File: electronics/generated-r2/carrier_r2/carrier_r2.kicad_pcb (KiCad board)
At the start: 2 copper layers, 100 x 140 mm, 40 parts, among them J1 EXTERNAL_3V3_FUSED_1A, J2 ENCODER_BANK_0, J3 ENCODER_BANK_1, J4 ENCODER_BANK_2, J5 ENCODER_BANK_3, J6 ADXL355_MODULE, J7 ODOMETER_3V3_ONLY, J8 ADC_BANK_FANOUT, J9 INTERLOCK_GND_LIFT_PG_REMOTE_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, Q1 MMBT3904, U1 Raspberry_Pi_Pico_USB_powered, U2 SN74LVC244APWR, U3 SN74LVC244APWR, U4 SN74LVC125AD_IOFF

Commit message: build(r2): publish final routed electronics and checks [skip ci]
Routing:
- net GND: track 552.7 -> 481.0 mm
- net P_MOSI1: track 108.6 -> 129.9 mm
- net LIFT_STOWED_N: track 108.3 -> 90.8 mm, vias 0 -> 1
- net SENS_3V3: track 294.4 -> 281.1 mm, vias 1 -> 2
- net MISO0: track 96.3 -> 85.4 mm, vias 1 -> 2
- net ADC_CS3: track 65.6 -> 75.8 mm
- net ADC_CS2: track 65.1 -> 73.8 mm, vias 1 -> 3
- net MISO0_RAW: track 110.2 -> 118.5 mm, vias 3 -> 1
- net P_SCK1: track 112.6 -> 105.2 mm
- net ADC_CS1: track 64.7 -> 70.6 mm, vias 1 -> 3
- net POWER_GOOD: track 105.1 -> 110.9 mm, vias 0 -> 1
- net ADC_CS0: track 68.5 -> 74.1 mm
- net P_CS2: track 43.4 -> 48.9 mm
- net PICO_3V3: track 192.2 -> 188.6 mm
- net CS3: track 52.8 -> 55.8 mm
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
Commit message: build(r2): publish four routed boards and checks [skip ci]
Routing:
- net MISO0_RAW: track 118.5 -> 150.0 mm, vias 1 -> 0
- net P_MOSI1: track 129.9 -> 106.6 mm, vias 1 -> 2
- net ADC_CS1: track 70.6 -> 84.1 mm, vias 3 -> 1
- net PICO_3V3: track 188.6 -> 176.4 mm
- net MISO0: track 85.4 -> 96.3 mm, vias 2 -> 1
- net P_SCK1: track 105.2 -> 114.6 mm
- net LIFT_STOWED_N: track 90.8 -> 99.2 mm
- net CS2: track 46.5 -> 54.7 mm
- net SENS_3V3: track 281.1 -> 273.2 mm, vias 2 -> 1
- net P_CS2: track 48.9 -> 42.1 mm
- net CS_ADXL: track 79.4 -> 84.3 mm
- net ADC_CS3: track 75.8 -> 71.9 mm
- net CS1: track 47.2 -> 50.1 mm
- net CS3: track 55.8 -> 53.1 mm
- net ADC_CS0: track 74.1 -> 71.6 mm, vias 1 -> 0
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
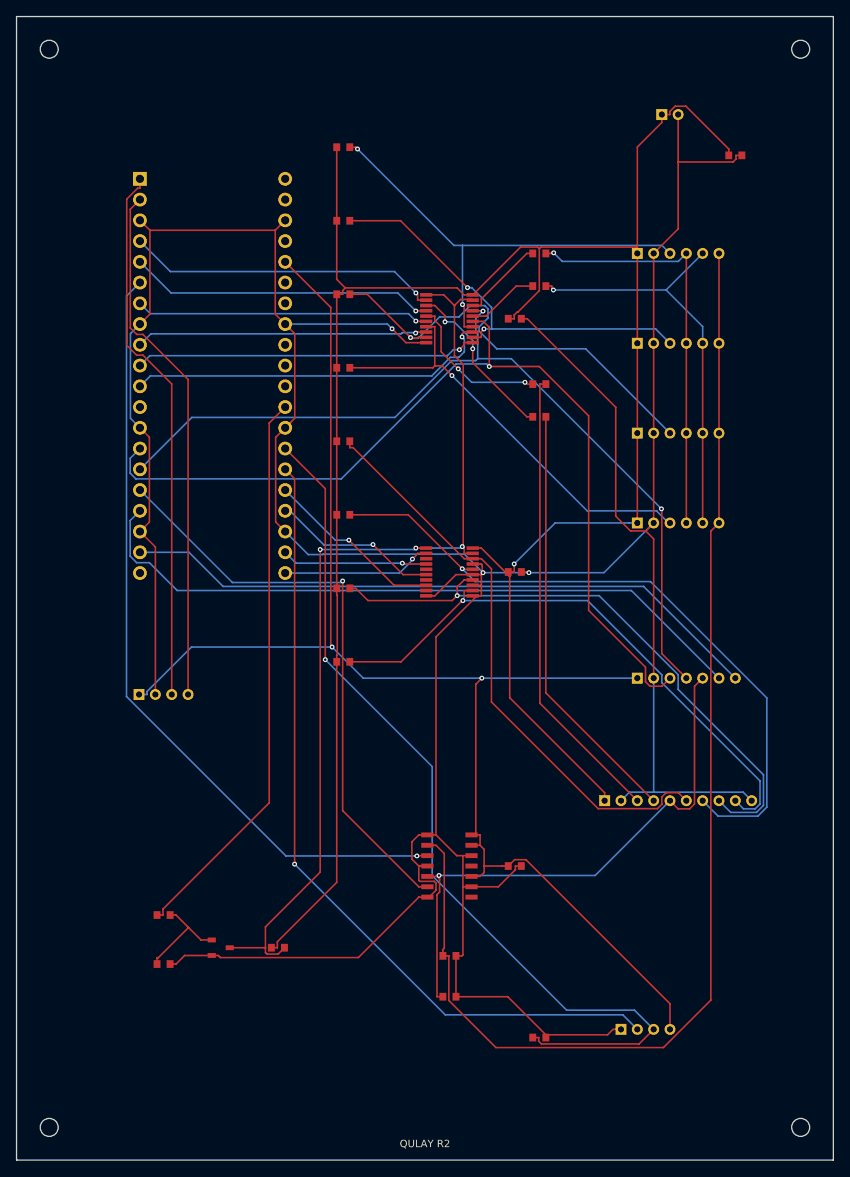
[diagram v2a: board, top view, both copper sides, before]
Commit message: build(r2): publish verified four-board electronics baseline [skip ci]
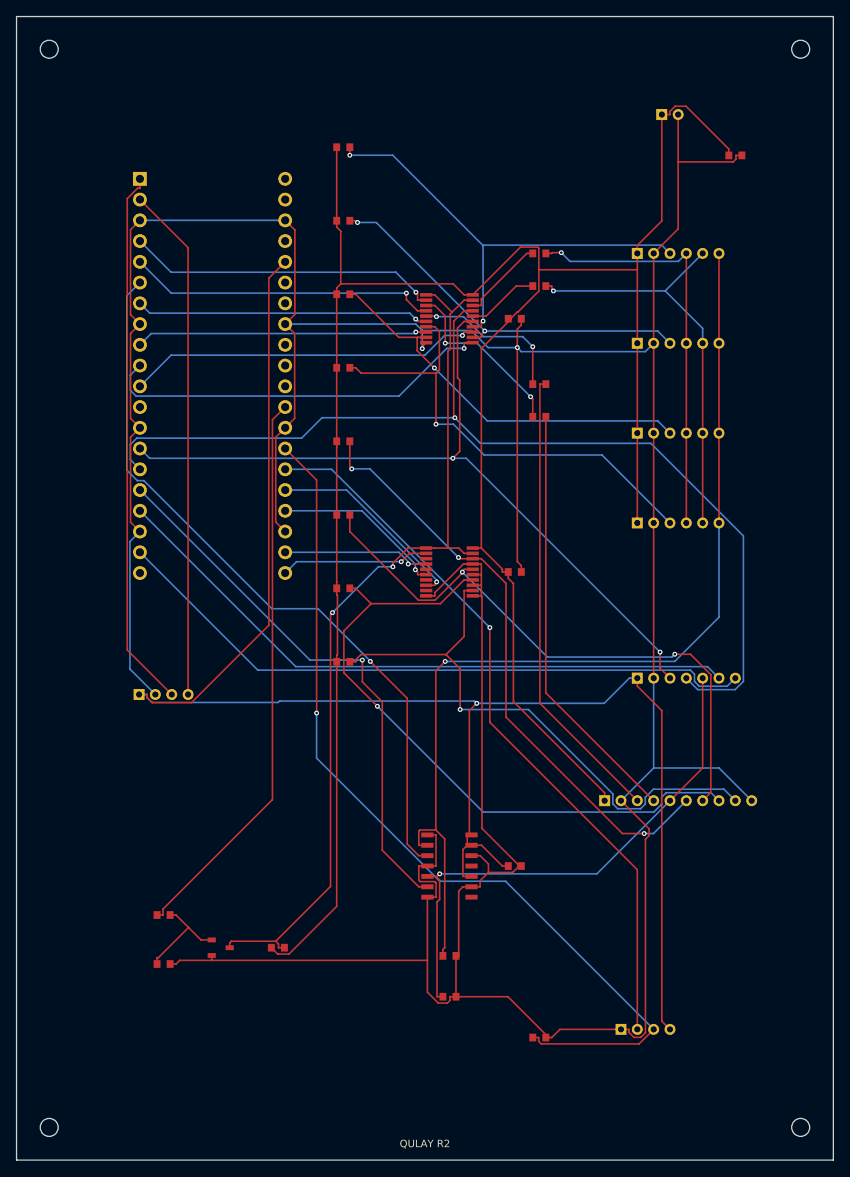
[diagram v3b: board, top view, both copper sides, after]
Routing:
- net MISO0_RAW: track 150.0 -> 122.3 mm, vias 0 -> 1
- net GND: track 481.3 -> 508.1 mm, vias 3 -> 2
- net PICO_3V3: track 176.4 -> 203.0 mm, vias 2 -> 1
- net P_MOSI1: track 106.6 -> 126.4 mm, vias 2 -> 1
- net P_SCK1: track 114.6 -> 96.3 mm, vias 1 -> 2
- net SENS_3V3: track 273.2 -> 285.2 mm, vias 1 -> 0
- net ADC_CS1: track 84.1 -> 74.0 mm, vias 1 -> 2
- net LIFT_STOWED_N: track 99.2 -> 89.8 mm
- net OE_SENS_N: track 116.6 -> 108.3 mm, vias 3 -> 2
- net P_CS2: track 42.1 -> 48.8 mm
- net ADC_CS2: track 75.1 -> 81.7 mm
- net CS2: track 54.7 -> 48.3 mm
- net MISO0: track 96.3 -> 90.5 mm
- net CS_ADXL: track 84.3 -> 79.4 mm
- net CS3: track 53.1 -> 57.9 mm
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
